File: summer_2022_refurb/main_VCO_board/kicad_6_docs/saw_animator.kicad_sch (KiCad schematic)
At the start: 22 parts, among them U6 TL074, U7 LM311

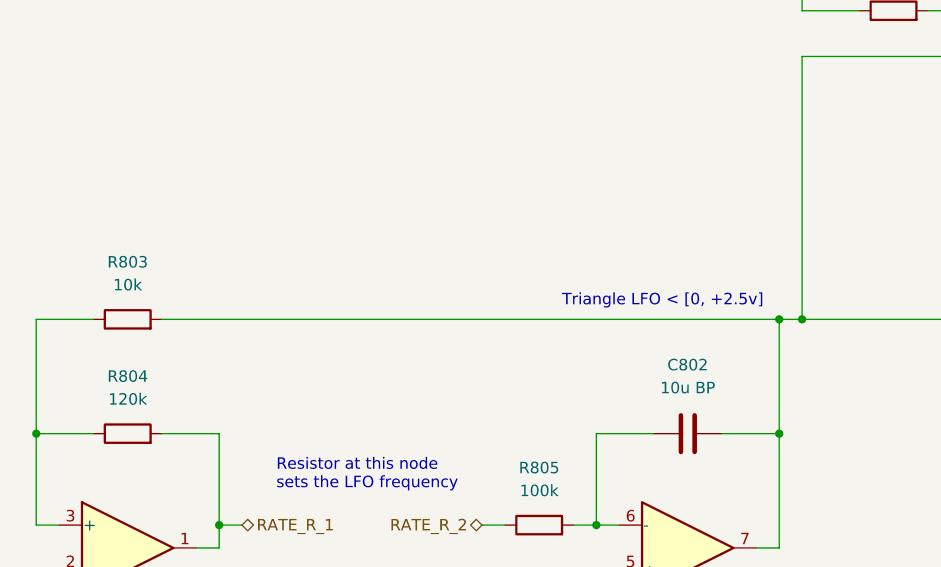
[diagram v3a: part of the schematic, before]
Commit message: Initial VCO layout
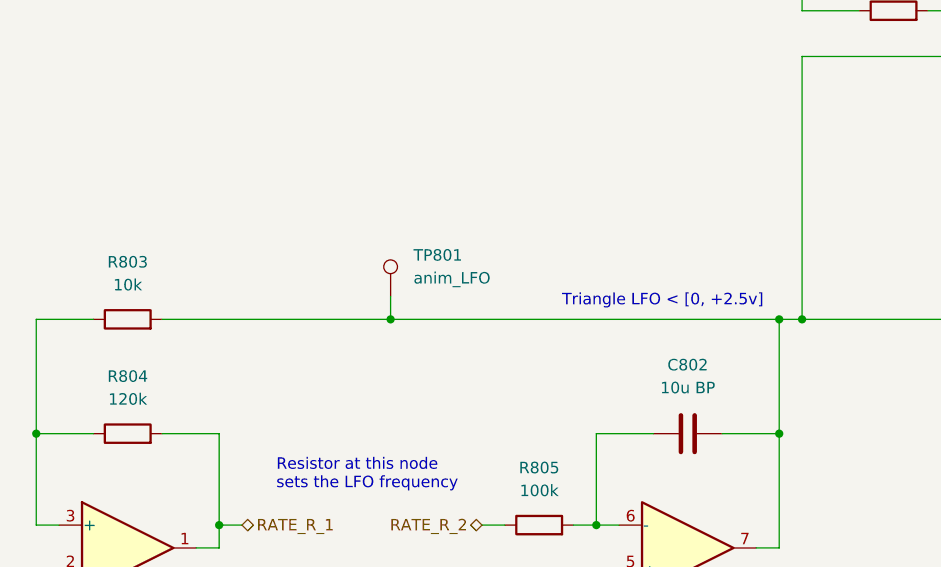
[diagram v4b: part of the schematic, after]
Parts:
- added TP801: anim_LFO, TestPoint:TestPoint_Keystone_5000-5004_Miniature, symbol Connector:TestPoint
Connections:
- net at C802.2, R803.2, R813.2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: now also TP801.1
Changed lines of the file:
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@@
   (junction (at 208.28 73.66) (diameter 0) (color 0 0 0 0)
+  )
+  (junction (at 77.47 128.27) (diameter 0) (color 0 0 0 0)
   )
   (junction (at 140.97 46.99) (diameter 0) (color 0 0 0 0)
@@
     (stroke (width 0) (type default) (color 0 0 0 0))
   )
+  (wire (pts (xy 77.47 125.73) (xy 77.47 128.27))
+    (stroke (width 0) (type default) (color 0 0 0 0))
+  )
   (wire (pts (xy 140.97 46.99) (xy 140.97 36.83))
     (stroke (width 0) (type default) (color 0 0 0 0))
@@
     (stroke (width 0) (type default) (color 0 0 0 0))
   )
+  (wire (pts (xy 77.47 128.27) (xy 52.07 128.27))
+    (stroke (width 0) (type default) (color 0 0 0 0))
+  )
   (wire (pts (xy 217.17 52.07) (xy 219.71 52.07))
     (stroke (width 0) (type default) (color 0 0 0 0))
@@
     (stroke (width 0) (type default) (color 0 0 0 0))
   )
-  (wire (pts (xy 120.65 128.27) (xy 52.07 128.27))
+  (wire (pts (xy 120.65 128.27) (xy 77.47 128.27))
     (stroke (width 0) (type default) (color 0 0 0 0))
   )
@@
     (effects (font (size 1.27 1.27)) (justify right))
   )
+  (symbol (lib_id "Connector:TestPoint") (at 77.47 125.73 0) (unit 1)
+    (in_bom no) (on_board yes) (fields_autoplaced)
+    (property "Reference" "TP801" (id 0) (at 80.01 121.1579 0)
+      (effects (font (size 1.27 1.27)) (justify left))
+    )
+    (property "Value" "anim_LFO" (id 1) (at 80.01 123.6979 0)
+      (effects (font (size 1.27 1.27)) (justify left))
+    )
+    (property "Footprint" "TestPoint:TestPoint_Keystone_5000-5004_Miniature" (id 2) (at 82.55 125.73 0)
+      (effects (font (size 1.27 1.27)) hide)
+    )
+    (property "Datasheet" "~" (id 3) (at 82.55 125.73 0)
+      (effects (font (size 1.27 1.27)) hide)
+    )
+    (pin "1")
+  )
   (symbol (lib_id "Device:R") (at 201.93 128.27 270) (mirror x) (unit 1)
